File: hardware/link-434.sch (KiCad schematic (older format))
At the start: 57 parts, among them J1 USB_A_PLUG, J2 SMA, J3 Conn_01x04, J4 Conn_01x05, SW1 SW_Push, U1 MAX7032ATJ+, U2 EFM8UB31F40G, Y1 17.63416MHz, 4.5pF load cap., Y2 SFECV10M7JA00

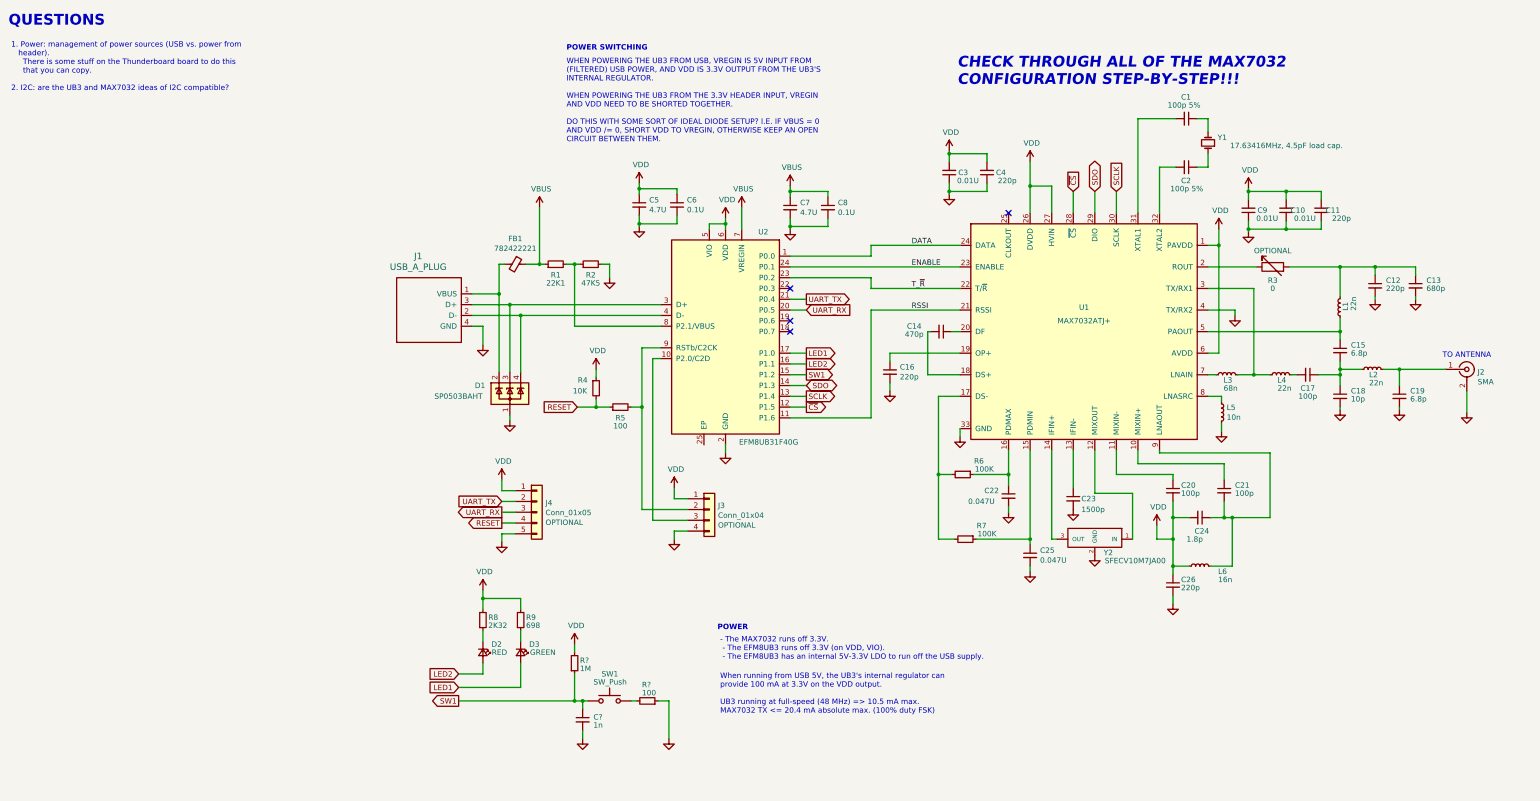
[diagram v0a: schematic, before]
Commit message: Schematic reorganisation
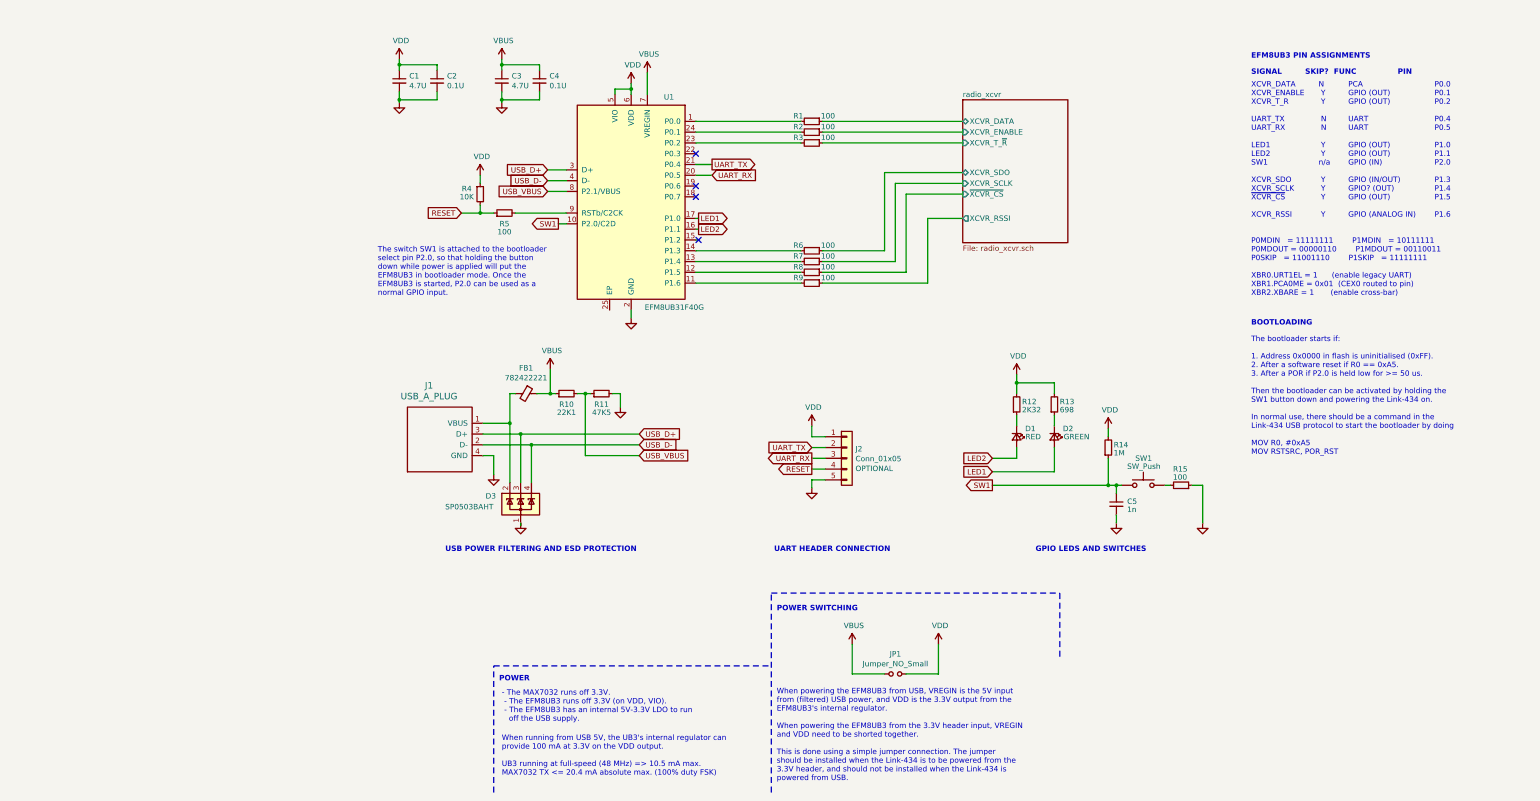
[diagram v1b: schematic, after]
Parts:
- removed C1, C2: 100p 5%, symbol link-434:C_Small
- removed C10, C3, C9: 0.01U, symbol link-434:C_Small
- removed C11, C12, C16, C26, C4: 220p, symbol link-434:C_Small
- removed C13: 680p, symbol link-434:C_Small
- removed C14: 470p, symbol link-434:C_Small
- removed C15, C19: 6.8p, symbol link-434:C_Small
- removed C17, C20, C21: 100p, symbol link-434:C_Small
- removed C18: 10p, symbol link-434:C_Small
- removed C22, C25: 0.047U, symbol link-434:C_Small
- removed C23: 1500p, symbol link-434:C_Small
- removed C24: 1.8p, symbol link-434:C_Small
- removed J2: SMA, symbol link-434:Conn_Coaxial
- removed J3: Conn_01x04, symbol link-434:Conn_01x04
- removed L1, L2, L4: 22n, symbol link-434:L_Small
- removed L3: 68n, symbol link-434:L_Small
- removed L5: 10n, symbol link-434:L_Small
- removed L6: 16n, symbol link-434:L_Small
- removed R3: 0, symbol Device:R_Variable
- removed U1: MAX7032ATJ+, symbol link-434:MAX7032ATJ+
- removed Y1: 17.63416MHz, 4.5pF load cap., symbol link-434:Crystal_Small
- removed Y2: SFECV10M7JA00, symbol link-434:SFECV10M7JA00-R0
- added JP1: Jumper_NO_Small, symbol link-434:Jumper_NO_Small
- added R1, R2, R3, R8, R9: 100, symbol link-434:R_Small
- R6, R7: value 100K -> 100
- gave numbers to parts that had none: 3
- renumbered C5 to C1, C6 to C2, C7 to C3, C8 to C4, D2 to D1, D3 to D2, D1 to D3, J4 to J2, R1 to R10, R2 to R11, R8 to R12, R9 to R13, U2 to U1
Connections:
- net SCLK is gone; now on an unnamed net: U1.13 (P1.4)
- net SW1: now also U1.10 (P2.0/C2D); no longer U1.15 (P1.2)
- net VBUS: now also JP1.1
- net VDD: now also JP1.2
- net USB_D+: now reaches D3.3 (K), J1.3 (D+), U1.3 (D+)
- net USB_D-: now reaches D3.4 (K), J1.2 (D-), U1.4 (D-)
- net USB_VBUS: now reaches R10.2, R11.1, U1.8 (P2.1/VBUS)
- net radio_xcvr/XCVR_SCLK: now reaches R7.1
- net radio_xcvr/XCVR_SDO: now reaches R6.1
- net at R7.2: no longer R6.2
- net DATA: no longer names the net of U1.1 (P0.0)
- net DATA: now also R1.2
- net ENABLE: no longer names the net of U1.24 (P0.1)
- net ENABLE: now also R2.2
- net RSSI: no longer names the net of U1.11 (P1.6)
- net RSSI: now also R9.2
- net SDO: no longer names the net of U1.14 (P1.3)
- net SDO: now also R6.2
- net T_~R: no longer names the net of U1.23 (P0.2)
- net T_~R: now also R3.2
- net ~CS: no longer names the net of U1.12 (P1.5)
- net ~CS: now also R8.2
- new net radio_xcvr/XCVR_DATA: R1.1
- new net radio_xcvr/XCVR_ENABLE: R2.1
- new net radio_xcvr/XCVR_RSSI: R9.1
- new net radio_xcvr/XCVR_T_~R: R3.1
- new net radio_xcvr/~XCVR_CS: R8.1
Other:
- note added: "- The MAX7032 runs off 3.3V.\n - The EFM8UB3 runs off 3.3V (on VDD, VIO).\n - The EFM8UB3 has an internal 5V-3.3V LDO to run\n off the USB supply."
- note added: "BOOTLOADING"
- note added: "EFM8UB3 PIN ASSIGNMENTS"
- note added: "GPIO LEDS AND SWITCHES"
- note added: "N\n Y\n Y\n\n N\n N\n\n Y\n Y\nn/a\n\n Y\n Y\n Y\n\n Y"
- note added: "P0.0\nP0.1\nP0.2\n\nP0.4\nP0.5\n\nP1.0\nP1.1\nP2.0\n\nP1.3\nP1.4\nP1.5\n\nP1.6"
- note added: "P0MDIN = 11111111 P1MDIN = 10111111\nP0MDOUT = 00000110 P1MDOUT = 00110011\nP0SKIP = 11001110 P1SKIP = 11111111\n\nXBR0.URT1EL = 1 (enable legacy UART)\nXBR1.PCA0ME = 0x01 (CEX0 routed to pin)\nXBR2.XBARE = 1 (enable cross-bar)\n"
- note added: "PCA\nGPIO (OUT)\nGPIO (OUT)\n\nUART\nUART\n\nGPIO (OUT)\nGPIO (OUT)\nGPIO (IN)\n\nGPIO (IN/OUT)\nGPIO? (OUT)\nGPIO (OUT)\n\nGPIO (ANALOG IN)\n"
- note added: "SIGNAL SKIP? FUNC PIN"
- note added: "The bootloader starts if:\n\n1. Address 0x0000 in flash is uninitialised (0xFF).\n2. After a software reset if R0 == 0xA5.\n3. After a POR if P2.0 is held low for >= 50 us.\n\nThen the bootloader can be activated by holding the\nSW1 button down and powering the Link-434 on.\n\nIn normal use, there should be a command in the\nLink-434 USB protocol to start the bootloader by doing\n\nMOV R0, #0xA5\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"
- note added: "The switch SW1 is attached to the bootloader\nselect pin P2.0, so that holding the button\ndown while power is applied will put the\nEFM8UB3 in bootloader mode. Once the\nEFM8UB3 is started, P2.0 can be used as a\nnormal GPIO input."
- note added: "UART HEADER CONNECTION"
- note added: "USB POWER FILTERING AND ESD PROTECTION"
- note added: "When powering the EFM8UB3 from USB, VREGIN is the 5V input\nfrom (filtered) USB power, and VDD is the 3.3V output from the\nEFM8UB3's internal regulator.\n\nWhen powering the EFM8UB3 from the 3.3V header input, VREGIN\nand VDD need to be shorted together.\n\nThis is done using a simple jumper connection. The jumper\nshould be installed when the Link-434 is to be powered from the\n3.3V header, and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"
- note added: "XCVR_DATA\nXCVR_ENABLE\nXCVR_T_R\n\nUART_TX\nUART_RX\n\nLED1\nLED2\nSW1\n\nXCVR_SDO\nXCVR_SCLK\n~XCVR_CS~\n\nXCVR_RSSI\n"
- note removed: "- The MAX7032 runs off 3.3V.\n - The EFM8UB3 runs off 3.3V (on VDD, VIO).\n - The EFM8UB3 has an internal 5V-3.3V LDO to run off the USB supply."
- note removed: "1. Power: management of power sources (USB vs. power from\n header).\n There is some stuff on the Thunderboard board to do this\n that you can copy.\n\n2. I2C: are the UB3 and MAX7032 ideas of I2C compatible?\n"
- note removed: "CHECK THROUGH ALL OF THE MAX7032\nCONFIGURATION STEP-BY-STEP!!!"
- note removed: "QUESTIONS"
- note removed: "TO ANTENNA"
- note removed: "WHEN POWERING THE UB3 FROM USB, VREGIN IS 5V INPUT FROM\n(FILTERED) USB POWER, AND VDD IS 3.3V OUTPUT FROM THE UB3'S\nINTERNAL REGULATOR.\n\nWHEN POWERING THE UB3 FROM THE 3.3V HEADER INPUT, VREGIN\nAND VDD NEED TO BE SHORTED TOGETHER.\n\nDO THIS WITH SOME SORT OF IDEAL DIODE SETUP? I.E. IF VBUS = 0\nAND VDD /= 0, SHORT VDD TO VREGIN, OTHERWISE KEEP AN OPEN\nCIRCUIT BETWEEN THEM."
- moved on the sheet: C1, C2, C3, C4, C5, D1, D2, D3, FB1, J1, J2, R10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

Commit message: Schematic checklist
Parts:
- removed R1, R15, R2, R3, R6, R7, R8, R9: 100, symbol link-434:R_Small
- added RN1, RN2: 100, link-434:CAT16101J4LF, symbol link-434:R_Pack04_Split
- C1, C2, C3, C4, C5: footprint (none) -> link-434:C_0402_1005Metric
- D1, D2: footprint (none) -> link-434:LED_0805_2012Metric
- D3: footprint Package_TO_SOT_SMD:SOT-143 -> link-434:SOT-143; Link (none) -> https://www.mouser.at/ProductDetail/Littelfuse/SP0503BAHTG?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; MPN (none) -> SP0503BAHTG
- FB1: footprint (none) -> link-434:Ferrite_0402_1005Metric; Link (none) -> https://www.mouser.at/ProductDetail/Wurth-Elektronik/782422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; MPN (none) -> 782422221
- J1: footprint (none) -> link-434:usb-a-edge
- J2: footprint (none) -> link-434:PinHeader_1x05_P2.54mm_Vertical
- JP1: footprint (none) -> link-434:PinHeader_1x02_P2.54mm_Vertical
- R10, R11, R12, R13, R14, R4, R5: footprint (none) -> link-434:R_0402_1005Metric
- SW1: footprint (none) -> link-434:PTS526SM15SMTR2LFS; Link (none) -> https://www.mouser.at/ProductDetail/CK/PTS526-SM15-SMTR2-LFS; MPN (none) -> PTS526 SM15 SMTR2 LFS
- U1: footprint (none) -> link-434:QFN-24-1EP_4x4mm_P0.5mm_EP2.6x2.6mm_ThermalVias; Link (none) -> https://www.mouser.at/ProductDetail/Silicon-Labs/EFM8UB31F4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; MPN (none) -> EFM8UB31F40G-A-QFN24
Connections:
- net GND: now also U1.25 (EP), RN2.5 (R4.2)
- net LED1: now also D2.1 (K); no longer D2.2 (A)
- net LED2: now also D1.1 (K); no longer D1.2 (A)
- net USB_D+: now also D3.2 (K); no longer D3.3 (K)
- net USB_D-: now also D3.3 (K); no longer D3.4 (K)
- net radio_xcvr/XCVR_DATA: now also RN1.8 (R1.2)
- net radio_xcvr/XCVR_ENABLE: now also RN1.7 (R2.2)
- net radio_xcvr/XCVR_RSSI: now also RN2.6 (R3.2)
- net radio_xcvr/XCVR_SCLK: now also RN2.8 (R1.2)
- net radio_xcvr/XCVR_SDO: now also RN1.5 (R4.2)
- net radio_xcvr/XCVR_T_~R: now also RN1.6 (R3.2)
- net radio_xcvr/~XCVR_CS: now also RN2.7 (R2.2)
- net at U1.1 (P0.0): now also RN1.1 (R1.1)
- net at U1.11 (P1.6): now also RN2.3 (R3.1)
- net at U1.12 (P1.5): now also RN2.2 (R2.1)
- net at U1.13 (P1.4): now also RN2.1 (R1.1)
- net at U1.14 (P1.3): now also RN1.4 (R4.1)
- net at U1.23 (P0.2): now also RN1.3 (R3.1)
- net at U1.24 (P0.1): now also RN1.2 (R2.1)
- net at FB1.2, J1.1 (VBUS): now also D3.4 (K); no longer D3.2 (K)
- net at R12.1: now also D1.2 (A); no longer D1.1 (K)
- net at R13.1: now also D2.2 (A); no longer D2.1 (K)
- net at SW1.2: now also RN2.4 (R4.1)
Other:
- note added: "TODO: REORDER PINS HERE"
- moved on the sheet: D1, D2

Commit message: Tidying
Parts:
- RN1, RN2: Link (none) -> https://www.mouser.at/ProductDetail/Bourns/CAT16-101J4LF; MPN (none) -> CAT16-101J4LF
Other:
- note removed: "TODO: REORDER PINS HERE"
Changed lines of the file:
@@
 Wire Wire Line
 	3000 3350 3000 3325
-Text Notes 2200 5225 0    50   Italic 0
-TODO: REORDER PINS HERE
 Wire Wire Line
 	1875 4925 1875 4475
@@
 F 1 "100" V 4625 3000 50  0000 C CNN
 F 2 "link-434:CAT16101J4LF" V 4595 2775 50  0001 C CNN
-F 3 "~" H 4675 2775 50  0001 C CNN
+F 3 "https://www.mouser.at/datasheet/2/54/CATCAY-777361.pdf" H 4675 2775 50  0001 C CNN
+F 4 "https://www.mouser.at/ProductDetail/Bourns/CAT16-101J4LF" H 4675 2775 50  0001 C CNN "Link"
+F 5 "CAT16-101J4LF" H 4675 2775 50  0001 C CNN "MPN"
 	4    4675 2775
 	0    1    1    0
@@
 F 1 "100" V 4625 3100 50  0000 C CNN
 F 2 "link-434:CAT16101J4LF" V 4595 2875 50  0001 C CNN
-F 3 "~" H 4675 2875 50  0001 C CNN
+F 3 "https://www.mouser.at/datasheet/2/54/CATCAY-777361.pdf" H 4675 2875 50  0001 C CNN
+F 4 "https://www.mouser.at/ProductDetail/Bourns/CAT16-101J4LF" H 4675 2875 50  0001 C CNN "Link"
+F 5 "CAT16-101J4LF" H 4675 2875 50  0001 C CNN "MPN"
 	1    4675 2875
 	0    1    1    0
@@
 F 1 "100" V 4625 3200 50  0000 C CNN
 F 2 "link-434:CAT16101J4LF" V 4595 2975 50  0001 C CNN
-F 3 "~" H 4675 2975 50  0001 C CNN
+F 3 "https://www.mouser.at/datasheet/2/54/CATCAY-777361.pdf" H 4675 2975 50  0001 C CNN
+F 4 "https://www.mouser.at/ProductDetail/Bourns/CAT16-101J4LF" H 4675 2975 50  0001 C CNN "Link"
+F 5 "CAT16-101J4LF" H 4675 2975 50  0001 C CNN "MPN"
 	2    4675 2975
 	0    1    1    0
@@
 F 1 "100" V 4625 3300 50  0000 C CNN
 F 2 "link-434:CAT16101J4LF" V 4595 3075 50  0001 C CNN
-F 3 "~" H 4675 3075 50  0001 C CNN
+F 3 "https://www.mouser.at/datasheet/2/54/CATCAY-777361.pdf" H 4675 3075 50  0001 C CNN
+F 4 "https://www.mouser.at/ProductDetail/Bourns/CAT16-101J4LF" H 4675 3075 50  0001 C CNN "Link"
+F 5 "CAT16-101J4LF" H 4675 3075 50  0001 C CNN "MPN"
 	3    4675 3075
 	0    1    1    0
@@
 F 1 "100" V 4625 1800 50  0000 C CNN
 F 2 "link-434:CAT16101J4LF" V 4595 1575 50  0001 C CNN
-F 3 "~" H 4675 1575 50  0001 C CNN
+F 3 "https://www.mouser.at/datasheet/2/54/CATCAY-777361.pdf" H 4675 1575 50  0001 C CNN
+F 4 "https://www.mouser.at/ProductDetail/Bourns/CAT16-101J4LF" H 4675 1575 50  0001 C CNN "Link"
+F 5 "CAT16-101J4LF" H 4675 1575 50  0001 C CNN "MPN"
 	1    4675 1575
 	0    1    1    0
@@
 F 1 "100" V 4625 1900 50  0000 C CNN
 F 2 "link-434:CAT16101J4LF" V 4595 1675 50  0001 C CNN
-F 3 "~" H 4675 1675 50  0001 C CNN
+F 3 "https://www.mouser.at/datasheet/2/54/CATCAY-777361.pdf" H 4675 1675 50  0001 C CNN
+F 4 "https://www.mouser.at/ProductDetail/Bourns/CAT16-101J4LF" H 4675 1675 50  0001 C CNN "Link"
+F 5 "CAT16-101J4LF" H 4675 1675 50  0001 C CNN "MPN"
 	2    4675 1675
 	0    1    1    0
@@
 F 1 "100" V 4625 2000 50  0000 C CNN
 F 2 "link-434:CAT16101J4LF" V 4595 1775 50  0001 C CNN
-F 3 "~" H 4675 1775 50  0001 C CNN
+F 3 "https://www.mouser.at/datasheet/2/54/CATCAY-777361.pdf" H 4675 1775 50  0001 C CNN
+F 4 "https://www.mouser.at/ProductDetail/Bourns/CAT16-101J4LF" H 4675 1775 50  0001 C CNN "Link"
+F 5 "CAT16-101J4LF" H 4675 1775 50  0001 C CNN "MPN"
 	3    4675 1775
 	0    1    1    0
@@
 F 1 "100" V 8275 4950 50  0000 C CNN
 F 2 "link-434:CAT16101J4LF" V 8020 4950 50  0001 C CNN
-F 3 "~" H 8100 4950 50  0001 C CNN
+F 3 "https://www.mouser.at/datasheet/2/54/CATCAY-777361.pdf" H 8100 4950 50  0001 C CNN
+F 4 "https://www.mouser.at/ProductDetail/Bourns/CAT16-101J4LF" H 8100 4950 50  0001 C CNN "Link"
+F 5 "CAT16-101J4LF" H 8100 4950 50  0001 C CNN "MPN"
 	4    8100 4950
 	0    1    1    0
